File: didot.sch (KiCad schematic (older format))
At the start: 64 parts, among them J1 JST_BATTERY, U1 nice!nano

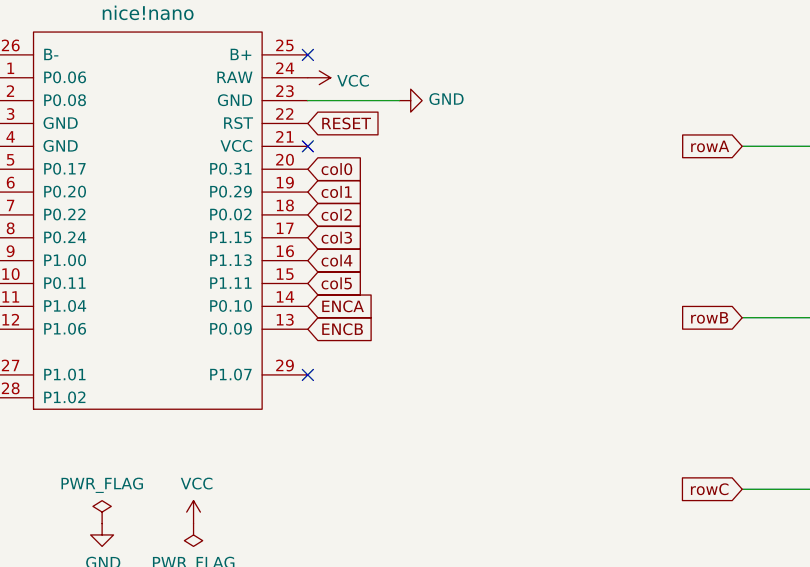
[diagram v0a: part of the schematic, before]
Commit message: Clean up routing, add JST pin markings
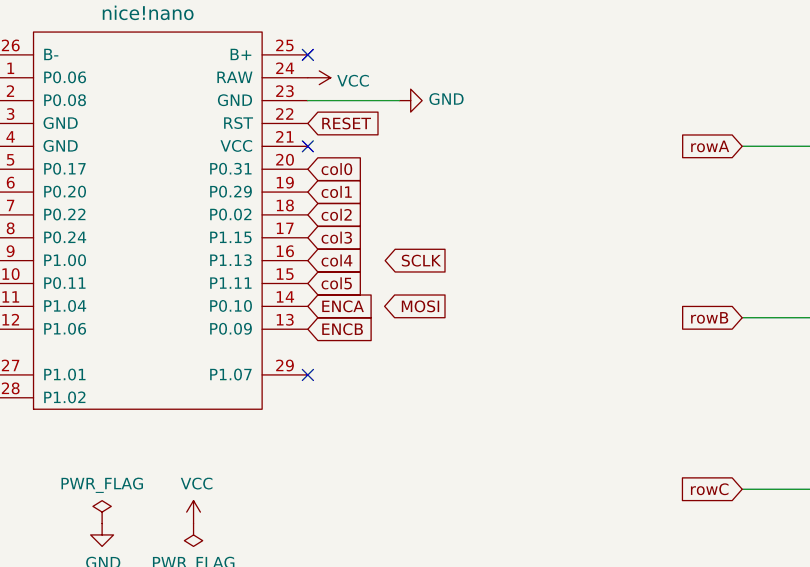
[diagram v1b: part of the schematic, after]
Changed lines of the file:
@@
 Wire Wire Line
 	5000 4500 5400 4500
+Text GLabel 3200 2500 0    50   Output ~ 0
+MOSI
+Text GLabel 3200 2300 0    50   Output ~ 0
+SCLK
 $EndSCHEMATC

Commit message: Complete v1.0 layout with footprints
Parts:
- added J2: Display Socket, Didot:1X09_ROUND_70, symbol Connector:Conn_01x09_Female
- added JP1: VCC, Didot:ReversibleDisplayJumper, symbol Jumper:SolderJumper_3_Open
- added JP2: CS, Didot:ReversibleDisplayJumper, symbol Jumper:SolderJumper_3_Open
- added JP3: SCLK, Didot:ReversibleDisplayJumper, symbol Jumper:SolderJumper_3_Open
- added JP4: GND, Didot:ReversibleDisplayJumper, symbol Jumper:SolderJumper_3_Open
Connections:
- net ENCA: now also U1.20 (P0.31); no longer U1.14 (P0.10)
- net ENCB: now also U1.19 (P0.29); no longer U1.13 (P0.09)
- net GND: now also JP4.2 (C)
- net MOSI: now also U1.7 (P0.22), J2.5 (Pin_5)
- net SCLK: now also U1.6 (P0.20), JP3.2 (C)
- net col0: now also U1.18 (P0.02); no longer U1.20 (P0.31)
- net col1: now also U1.17 (P1.15); no longer U1.19 (P0.29)
- net col2: now also U1.16 (P1.13); no longer U1.18 (P0.02)
- net col3: now also U1.15 (P1.11); no longer U1.17 (P1.15)
- net col4: now also U1.14 (P0.10); no longer U1.16 (P1.13)
- net col5: now also U1.13 (P0.09); no longer U1.15 (P1.11)
- net VCOM: now reaches U1.21 (VCC)
- net VCOM: now also JP1.2 (C)
- net CS: now reaches U1.5 (P0.17)
- net CS: now also JP2.2 (C)
- new net: J2.1 (Pin_1), JP1.1 (A)
- new net: J2.3 (Pin_3), JP4.1 (A)
- new net: J2.4 (Pin_4), JP2.3 (B), JP3.1 (A)
- new net: J2.6 (Pin_6), JP2.1 (A), JP3.3 (B)
- new net: J2.7 (Pin_7), JP4.3 (B)
- new net: J2.9 (Pin_9), JP1.3 (B)
- no-connect marks 12 -> 10
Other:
- note added: "Back"
- note added: "D0"
- note added: "D1"
- note added: "D10 / A10 / LF"
- note added: "D14 / LF"
- note added: "D15 / LF"
- note added: "D16 / LF"
- note added: "D18 / A0 / LF"
- note added: "D19 / A1 / LF"
- note added: "D2 / SDA"
- note added: "D20 / A2 / LF"
- note added: "D21 / A3 / LF"
- note added: "D3 / SCL"
- note added: "D4 / A6"
- note added: "D5"
- note added: "D6 / A7"
- note added: "D7"
- note added: "Front"
- note added: "LF / D8 / A8"
- note added: "LF / D9 / A9"
- note added: "Pin 1: front of board\nPin 3: back of board"
- moved on the sheet: SW_RESET1, U1
